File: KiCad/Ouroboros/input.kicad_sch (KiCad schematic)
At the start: 12 parts, among them J1 AudioJack2, SW1 SW_DPDT_x2, U1 Opamp_Quad

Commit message: Updating schematic
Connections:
- net GND: now also J1.S
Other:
- note added: "[2] Input"
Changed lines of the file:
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@@
+	)
+	(junction
+		(at 123.19 148.59)
+		(diameter 0)
+		(color 0 0 0 0)
 	)
 	(junction
@@
 		(color 0 0 0 0)
 	)
-	(junction
-		(at 115.57 148.59)
-		(diameter 0)
-		(color 0 0 0 0)
-	)
 	(wire
 		(pts
@@
 	(wire
 		(pts
-			(xy 115.57 148.59) (xy 115.57 158.75)
+			(xy 78.74 71.12) (xy 83.82 71.12)
+		)
+		(stroke
+			(width 0)
+			(type default)
+		)
+	)
+	(wire
+		(pts
+			(xy 123.19 148.59) (xy 123.19 158.75)
 		)
 		(stroke
@@
 	(wire
 		(pts
-			(xy 115.57 158.75) (xy 134.62 158.75)
+			(xy 123.19 158.75) (xy 134.62 158.75)
 		)
 		(stroke
@@
 			(font
 				(size 1.27 1.27)
+			)
+		)
+	)
+	(text "[2] Input\n"
+		(exclude_from_sim no)
+		(at 125.73 19.304 0)
+		(effects
+			(font
+				(size 5 5)
+				(color 132 0 0 1)
 			)
 		)
@@
 					(unit 1)
 				)
+			)
+		)
+	)
+	(symbol
+		(lib_id "power:GND")
+		(at 83.82 71.12 90)
+		(unit 1)
+		(exclude_from_sim no)
+		(in_bom yes)
+		(on_board yes)
+		(dnp no)
+		(fields_autoplaced yes)
+		(property "Reference" "#PWR033"
+			(at 90.17 71.12 0)
+			(effects
+				(font
+					(size 1.27 1.27)
+				)
+				(hide yes)
+			)
+		)
+		(property "Value" "GND"
+			(at 87.63 71.1199 90)
+			(effects
+				(font
+					(size 1.27 1.27)
+				)
+				(justify right)
+			)
+		)
+		(property "Footprint" ""
+			(at 83.82 71.12 0)
+			(effects
+				(font
+					(size 1.27 1.27)
+				)
+				(hide yes)
+			)
+		)
+		(property "Datasheet" ""
+			(at 83.82 71.12 0)
+			(effects
+				(font
+					(size 1.27 1.27)
+				)
+				(hide yes)
+			)
+		)
+		(property "Description" "Power symbol creates a global label with name \"GND\" , ground"
+			(at 83.82 71.12 0)
+			(effects
+				(font
+					(size 1.27 1.27)
+				)
+				(hide yes)
+			)
+		)
+		(pin "1"
+		)
+		(instances
+			(project ""
+				(path "/a2662f7c-8239-40ad-828c-dd886b1cb258/66c5e6da-8274-4bfc-b294-7d19b5ad631c"
+					(reference "#PWR033")
+					(unit 1)
+				)

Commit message: Linking nets
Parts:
- added J3, J4: AudioJack2, symbol Connector_Audio:AudioJack2
- added RV8: B10K, symbol Device:R_Potentiometer_Dual
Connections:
- net GND: now also J3.S, J4.S, RV8.1, RV8.4
- new net: J4.T, RV8.2
- new net: J3.T, RV8.5
- new net OUT_L: RV8.6
- new net OUT_R: RV8.3
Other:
- note added: "Output"
- note added: "[2] Input/Output"
- note removed: "[2] Input"
- moved on the sheet: C1, C2, C3, J1, R1, R2, R3, R4, R5, R6, SW1A, SW1B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

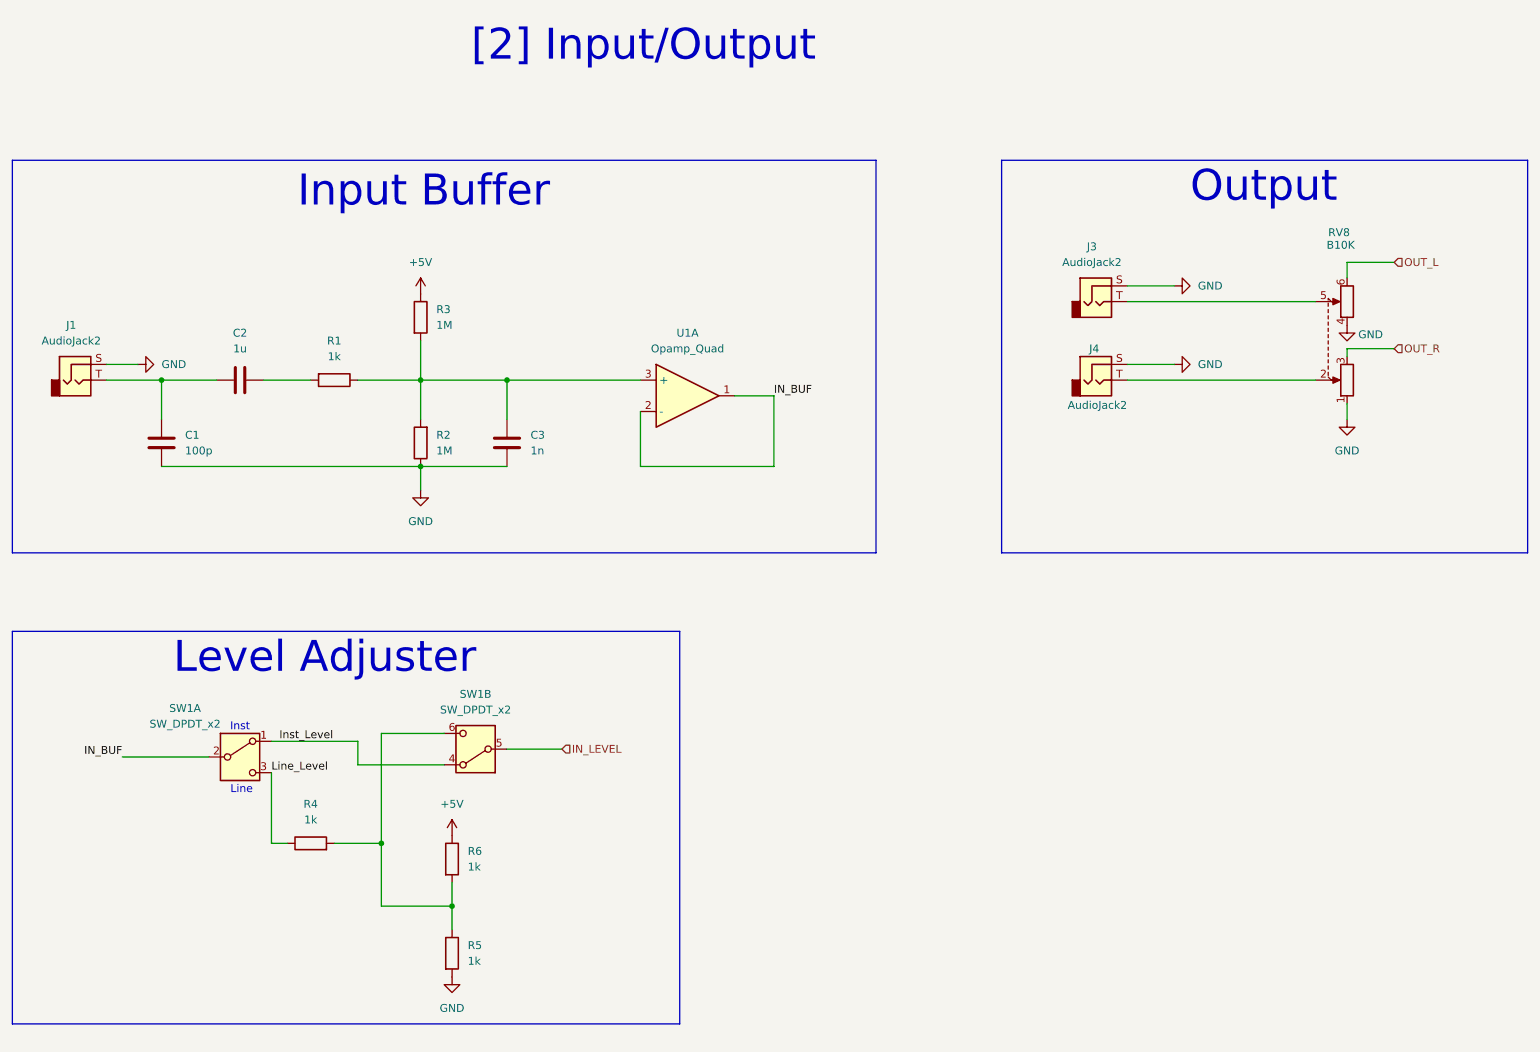
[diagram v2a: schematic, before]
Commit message: Updated schematic, started PCB
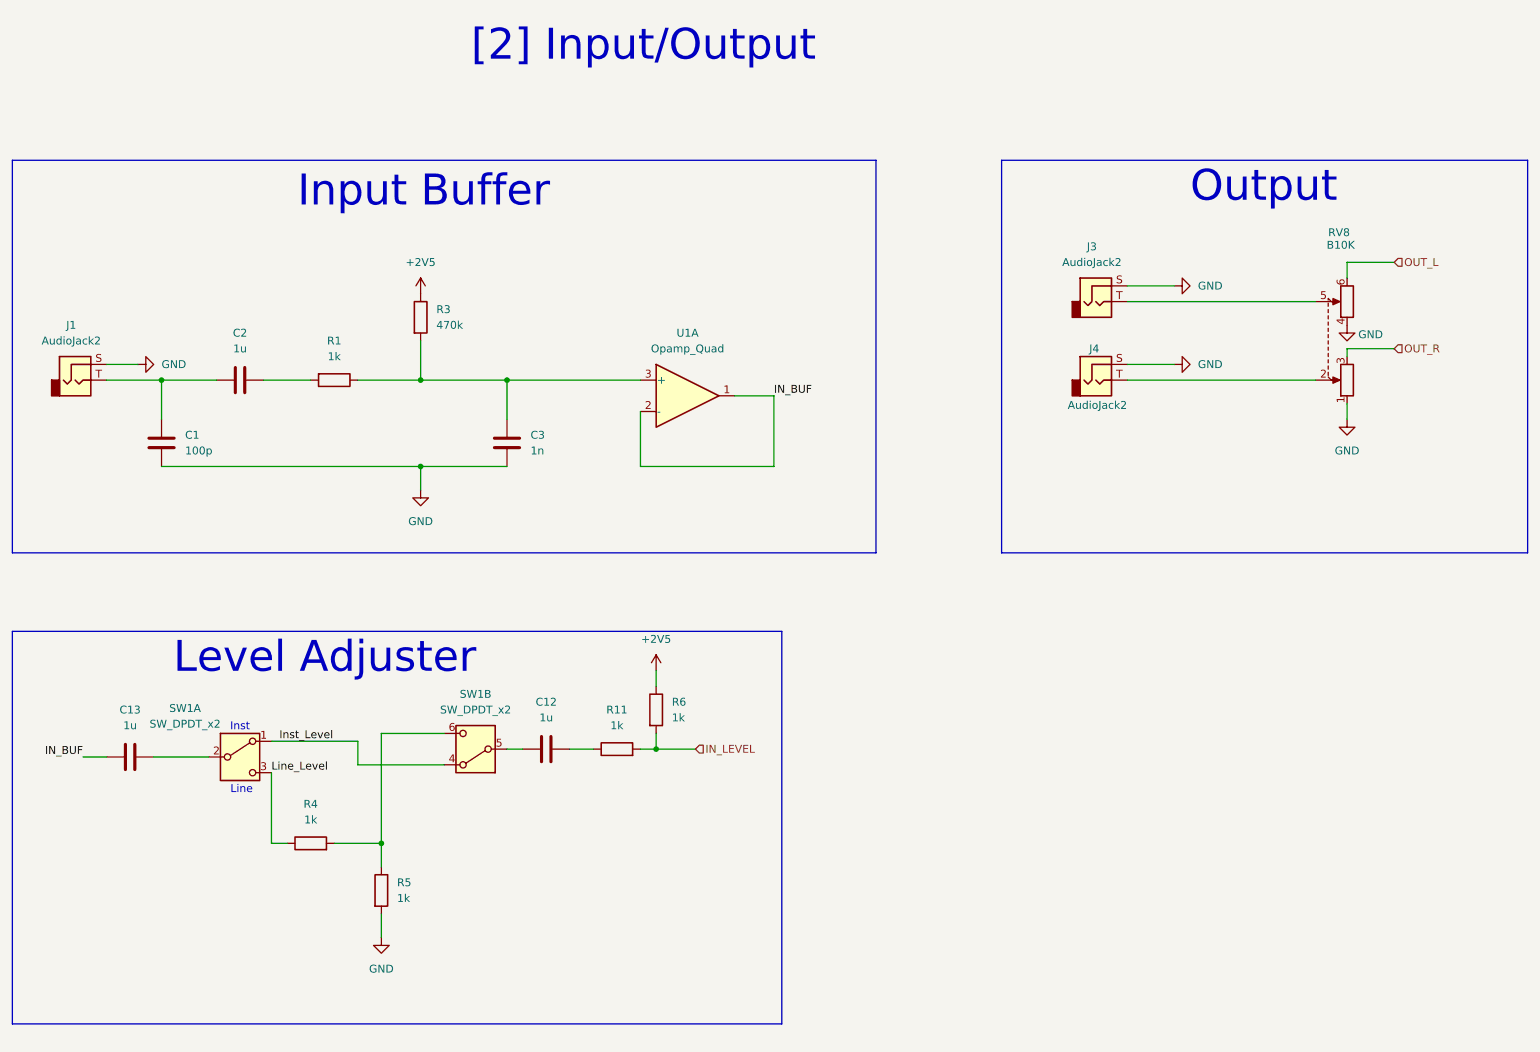
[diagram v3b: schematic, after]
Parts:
- removed R2: 1M, symbol Device:R
- added C12, C13: 1u, Capacitor_THT:C_Rect_L7.0mm_W3.5mm_P5.00mm, symbol Device:C
- added R11: 1k, Resistor_THT:R_Axial_DIN0207_L6.3mm_D2.5mm_P10.16mm_Horizontal, symbol Device:R
- C1, C3: footprint (none) -> Capacitor_THT:C_Rect_L7.0mm_W3.5mm_P5.00mm
- C2: footprint (none) -> Capacitor_THT:C_Rect_L7.0mm_W6.0mm_P5.00mm
- J1, J3, J4: footprint (none) -> Connector_Audio:Jack_6.35mm_Neutrik_NMJ4HFD2_Horizontal
- R1, R4, R5, R6: footprint (none) -> Resistor_THT:R_Axial_DIN0207_L6.3mm_D2.5mm_P10.16mm_Horizontal
- R3: value 1M -> 470k; footprint (none) -> Resistor_THT:R_Axial_DIN0207_L6.3mm_D2.5mm_P10.16mm_Horizontal
- RV8: footprint (none) -> Potentiometer_THT:Potentiometer_Alpha_RD902F-40-00D_Dual_Vertical
- SW1: footprint (none) -> Library:DPDT_Mini_Toggle
- U1: footprint (none) -> Package_DIP:DIP-14_W7.62mm_Socket; symbol Device:Opamp_Quad -> Amplifier_Operational:TL074
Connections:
- net IN_BUF: now also C13.1; no longer SW1.2 (B)
- net IN_LEVEL: now also R6.2, R11.2; no longer SW1.5 (B)
- net at R4.2, R5.1, SW1.6 (C): no longer R6.2
- net +5V renamed +2V5
- new net: C12.2, R11.1
- new net: C13.2, SW1.2 (B)
- new net: C12.1, SW1.5 (B)
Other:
- moved on the sheet: R5
